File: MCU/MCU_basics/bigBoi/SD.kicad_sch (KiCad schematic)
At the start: 3 parts, among them J3 DM3AT-SF-PEJM5_40_

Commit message: ERC resolving
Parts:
- C38, C39: footprint (none) -> Capacitor_SMD:C_0402_1005Metric
- J3: footprint DM3ATSFPEJM540 -> Nebula-footprints:DM3ATSFPEJM540
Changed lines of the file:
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@@
+	)
+	(junction
+		(at 101.6 102.87)
+		(diameter 0)
+		(color 0 0 0 0)
 	)
 	(junction
@@
 	(wire
 		(pts
-			(xy 107.95 102.87) (xy 93.98 102.87)
-		)
-		(stroke
-			(width 0)
-			(type default)
-		)
-	)
-	(wire
-		(pts
 			(xy 133.35 87.63) (xy 107.95 87.63)
 		)
@@
 	(wire
 		(pts
+			(xy 101.6 102.87) (xy 107.95 102.87)
+		)
+		(stroke
+			(width 0)
+			(type default)
+		)
+	)
+	(wire
+		(pts
+			(xy 101.6 102.87) (xy 93.98 102.87)
+		)
+		(stroke
+			(width 0)
+			(type default)
+		)
+	)
+	(wire
+		(pts
 			(xy 193.04 97.79) (xy 193.04 100.33)
 		)
@@
 		)
 	)
-	(label "DM3AT_SCLK_N"
-		(at 149.86 97.79 180)
+	(global_label "DM3AT_MISO_N"
+		(shape input)
+		(at 149.86 102.87 180)
+		(fields_autoplaced yes)
 		(effects
 			(font
 				(size 1.27 1.27)
 			)
-			(justify right bottom)
-		)
-	)
-	(label "DM3AT_MOSI_0"
+			(justify right)
+		)
+		(property "Intersheetrefs" "${INTERSHEET_REFS}"
+			(at 133.0258 102.87 0)
+			(hide yes)
+			(show_name no)
+			(do_not_autoplace no)
+			(effects
+				(font
+					(size 1.27 1.27)
+				)
+				(justify right)
+			)
+		)
+	)
+	(global_label "DM3AT_MOSI_0"
+		(shape input)
 		(at 149.86 92.71 180)
+		(fields_autoplaced yes)
 		(effects
 			(font
 				(size 1.27 1.27)
 			)
-			(justify right bottom)
-		)
-	)
-	(label "DM3AT_CS_N"
-		(at 149.86 90.17 180)
+			(justify right)
+		)
+		(property "Intersheetrefs" "${INTERSHEET_REFS}"
+			(at 133.1468 92.71 0)
+			(hide yes)
+			(show_name no)
+			(do_not_autoplace no)
+			(effects
+				(font
+					(size 1.27 1.27)
+				)
+				(justify right)
+			)
+		)
+	)
+	(global_label "DM3AT_CD_N"
+		(shape input)
+		(at 190.5 90.17 0)
+		(fields_autoplaced yes)
 		(effects
 			(font
 				(size 1.27 1.27)
 			)
-			(justify right bottom)
-		)
-	)
-	(label "DM3AT_CD_N"
-		(at 190.5 90.17 0)
+			(justify left)
+		)
+		(property "Intersheetrefs" "${INTERSHEET_REFS}"
+			(at 205.278 90.17 0)
+			(hide yes)
+			(show_name no)
+			(do_not_autoplace no)
+			(effects
+				(font
+					(size 1.27 1.27)
+				)
+				(justify left)
+			)
+		)
+	)
+	(global_label "DM3AT_SCLK_N"
+		(shape input)
+		(at 149.86 97.79 180)
+		(fields_autoplaced yes)
 		(effects
 			(font
 				(size 1.27 1.27)
 			)
-			(justify left bottom)
-		)
-	)
-	(label "DM3AT_MISO_N"
-		(at 149.86 102.87 180)
+			(justify right)
+		)
+		(property "Intersheetrefs" "${INTERSHEET_REFS}"
+			(at 132.8444 97.79 0)
+			(hide yes)
+			(show_name no)
+			(do_not_autoplace no)
+			(effects
+				(font
+					(size 1.27 1.27)
+				)
+				(justify right)
+			)
+		)
+	)
+	(global_label "DM3AT_CS_N"
+		(shape input)
+		(at 149.86 90.17 180)
+		(fields_autoplaced yes)
 		(effects
 			(font
 				(size 1.27 1.27)
 			)
-			(justify right bottom)
+			(justify right)
+		)
+		(property "Intersheetrefs" "${INTERSHEET_REFS}"
+			(at 135.1425 90.17 0)
+			(hide yes)
+			(show_name no)
+			(do_not_autoplace no)
+			(effects
+				(font
+					(size 1.27 1.27)
+				)
+				(justify right)
+			)
+		)
+	)
+	(symbol
+		(lib_id "power:PWR_FLAG")
+		(at 101.6 102.87 180)
+		(unit 1)
+		(body_style 1)
+		(exclude_from_sim no)
+		(in_bom yes)
+		(on_board yes)
+		(in_pos_files yes)
+		(dnp no)
+		(fields_autoplaced yes)
+		(property "Reference" "#FLG05"
+			(at 101.6 104.775 0)
+			(hide yes)
+			(show_name no)
+			(do_not_autoplace no)
+			(effects
+				(font
+					(size 1.27 1.27)
+				)
+			)
+		)
+		(property "Value" "PWR_FLAG"
+			(at 101.6 107.95 0)
+			(hide yes)
+			(show_name no)
+			(do_not_autoplace no)
+			(effects
+				(font
+					(size 1.27 1.27)
+				)
+			)
+		)
+		(property "Footprint" ""
+			(at 101.6 102.87 0)
+			(hide yes)
+			(show_name no)
+			(do_not_autoplace no)
+			(effects
+				(font
+					(size 1.27 1.27)
+				)
+			)
+		)
+		(property "Datasheet" ""
+			(at 101.6 102.87 0)
+			(hide yes)
+			(show_name no)
+			(do_not_autoplace no)
+			(effects
+				(font
+					(size 1.27 1.27)
+				)
+			)
+		)
+		(property "Description" "Special symbol for telling ERC where power comes from"
+			(at 101.6 102.87 0)
+			(hide yes)
+			(show_name no)
+			(do_not_autoplace no)
+			(effects
+				(font
+					(size 1.27 1.27)
+				)
+			)
+		)
+		(pin "1"
+		)
+		(instances
+			(project "bigBoi"
+				(path "/0a118c22-2522-42a6-b7a6-70c79326ece4/14471f1c-ba4e-4782-80ac-ae2b6b6eba47"
+					(reference "#FLG05")
+					(unit 1)
+				)
+			)
 		)
 	)
@@
 			)
 		)
-		(property "Footprint" ""
+		(property "Footprint" "Capacitor_SMD:C_0402_1005Metric"
 			(at 108.9152 99.06 0)
 			(hide yes)
@@
 			)
 		)
-		(property "Footprint" "DM3ATSFPEJM540"
+		(property "Footprint" "Nebula-footprints:DM3ATSFPEJM540"
 			(at 186.69 182.55 0)
 			(hide yes)
@@
 			)
 		)
-		(property "Footprint" ""
+		(property "Footprint" "Capacitor_SMD:C_0402_1005Metric"
 			(at 94.9452 99.06 0)
 			(hide yes)

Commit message: decoupling cap placement
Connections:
- net GND: now reaches J3.6 (VSS)
- net GND: now also J3.MP1, J3.MP2, J3.MP3, J3.MP4, J3.MP5
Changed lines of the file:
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@@
+	)
+	(symbol
+		(lib_id "power:GND")
+		(at 194.31 102.87 90)
+		(unit 1)
+		(body_style 1)
+		(exclude_from_sim no)
+		(in_bom yes)
+		(on_board yes)
+		(in_pos_files yes)
+		(dnp no)
+		(fields_autoplaced yes)
+		(property "Reference" "#PWR056"
+			(at 200.66 102.87 0)
+			(hide yes)
+			(show_name no)
+			(do_not_autoplace no)
+			(effects
+				(font
+					(size 1.27 1.27)
+				)
+			)
+		)
+		(property "Value" "GND"
+			(at 198.12 102.8699 90)
+			(hide yes)
+			(show_name no)
+			(do_not_autoplace no)
+			(effects
+				(font
+					(size 1.27 1.27)
+				)
+				(justify right)
+			)
+		)
+		(property "Footprint" ""
+			(at 194.31 102.87 0)
+			(hide yes)
+			(show_name no)
+			(do_not_autoplace no)
+			(effects
+				(font
+					(size 1.27 1.27)
+				)
+			)
+		)
+		(property "Datasheet" ""
+			(at 194.31 102.87 0)
+			(hide yes)
+			(show_name no)
+			(do_not_autoplace no)
+			(effects
+				(font
+					(size 1.27 1.27)
+				)
+			)
+		)
+		(property "Description" "Power symbol creates a global label with name \"GND\" , ground"
+			(at 194.31 102.87 0)
+			(hide yes)
+			(show_name no)
+			(do_not_autoplace no)
+			(effects
+				(font
+					(size 1.27 1.27)
+				)
+			)
+		)
+		(pin "1"
+		)
+		(instances
+			(project "bigBoi"
+				(path "/0a118c22-2522-42a6-b7a6-70c79326ece4/14471f1c-ba4e-4782-80ac-ae2b6b6eba47"
+					(reference "#PWR056")
+					(unit 1)
+				)
+			)
+		)
 	)
 	(symbol
@@
 			)
 		)
-		(property "Value" ""
+		(property "Value" "GND"
 			(at 130.81 100.3301 90)
+			(hide yes)
 			(show_name no)
 			(do_not_autoplace no)
@@
 					(unit 1)
 				)
-			)
-		)
-	)
-	(symbol
-		(lib_id "power:GND")
-		(at 194.31 102.87 90)
-		(unit 1)
-		(body_style 1)
-		(exclude_from_sim no)
-		(in_bom yes)
-		(on_board yes)
-		(in_pos_files yes)
-		(dnp no)
-		(fields_autoplaced yes)
-		(property "Reference" "#PWR056"
-			(at 200.66 102.87 0)
-			(hide yes)
-			(show_name no)
-			(do_not_autoplace no)
-			(effects
-				(font
-					(size 1.27 1.27)
-				)
-			)
-		)
-		(property "Value" ""
-			(at 198.12 102.8699 90)
-			(show_name no)
-			(do_not_autoplace no)
-			(effects
-				(font
-					(size 1.27 1.27)
-				)
-				(justify right)
-			)
-		)
-		(property "Footprint" ""
-			(at 194.31 102.87 0)
-			(hide yes)
-			(show_name no)
-			(do_not_autoplace no)
-			(effects
-				(font
-					(size 1.27 1.27)
-				)
-			)
-		)
-		(property "Datasheet" ""
-			(at 194.31 102.87 0)
-			(hide yes)
-			(show_name no)
-			(do_not_autoplace no)
-			(effects
-				(font
-					(size 1.27 1.27)
-				)
-			)
-		)
-		(property "Description" "Power symbol creates a global label with name \"GND\" , ground"
-			(at 194.31 102.87 0)
-			(hide yes)
-			(show_name no)
-			(do_not_autoplace no)
-			(effects
-				(font
-					(size 1.27 1.27)
-				)
-			)
-		)
-		(pin "1"
-		)
-		(instances
-			(project "bigBoi"
-				(path "/0a118c22-2522-42a6-b7a6-70c79326ece4/14471f1c-ba4e-4782-80ac-ae2b6b6eba47"
-					(reference "#PWR056")
-					(unit 1)
-				)

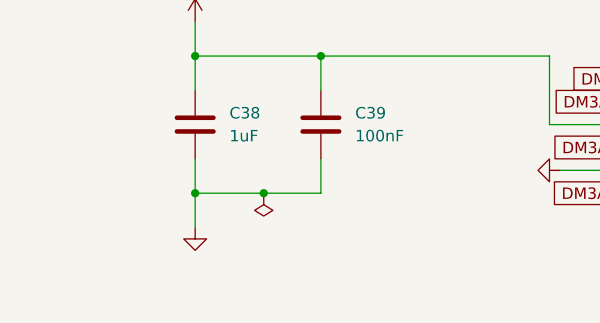
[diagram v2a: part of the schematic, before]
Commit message: Layout kategorier
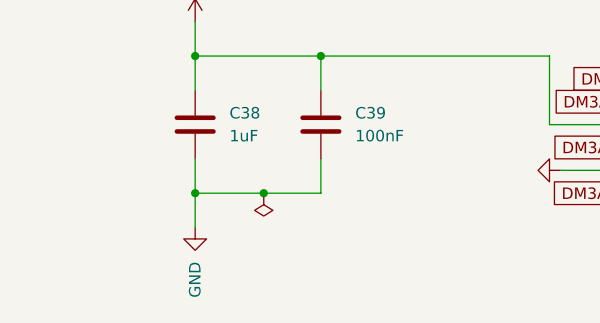
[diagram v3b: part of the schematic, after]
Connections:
- net GND: now also C38.2, C39.2
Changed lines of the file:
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@@
 			)
 		)
-		(property "Value" ""
+		(property "Value" "GND"
 			(at 93.9801 110.49 90)
 			(show_name no)
